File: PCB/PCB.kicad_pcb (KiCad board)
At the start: 4 copper layers, 104.1 x 104.1 mm, 113 parts, among them J1 Conn_01x06_Female, J2 09252306841, U1 Hx711, U10 Hx711, U11 Hx711, U12 Hx711, U13 74HC165, U15 LT3042xMSE, U16 74HC165, U2 Hx711, U3 Hx711, U4 Hx711, U5 Hx711, U6 Hx711, U7 Hx711, U8 Hx711, U9 Hx711

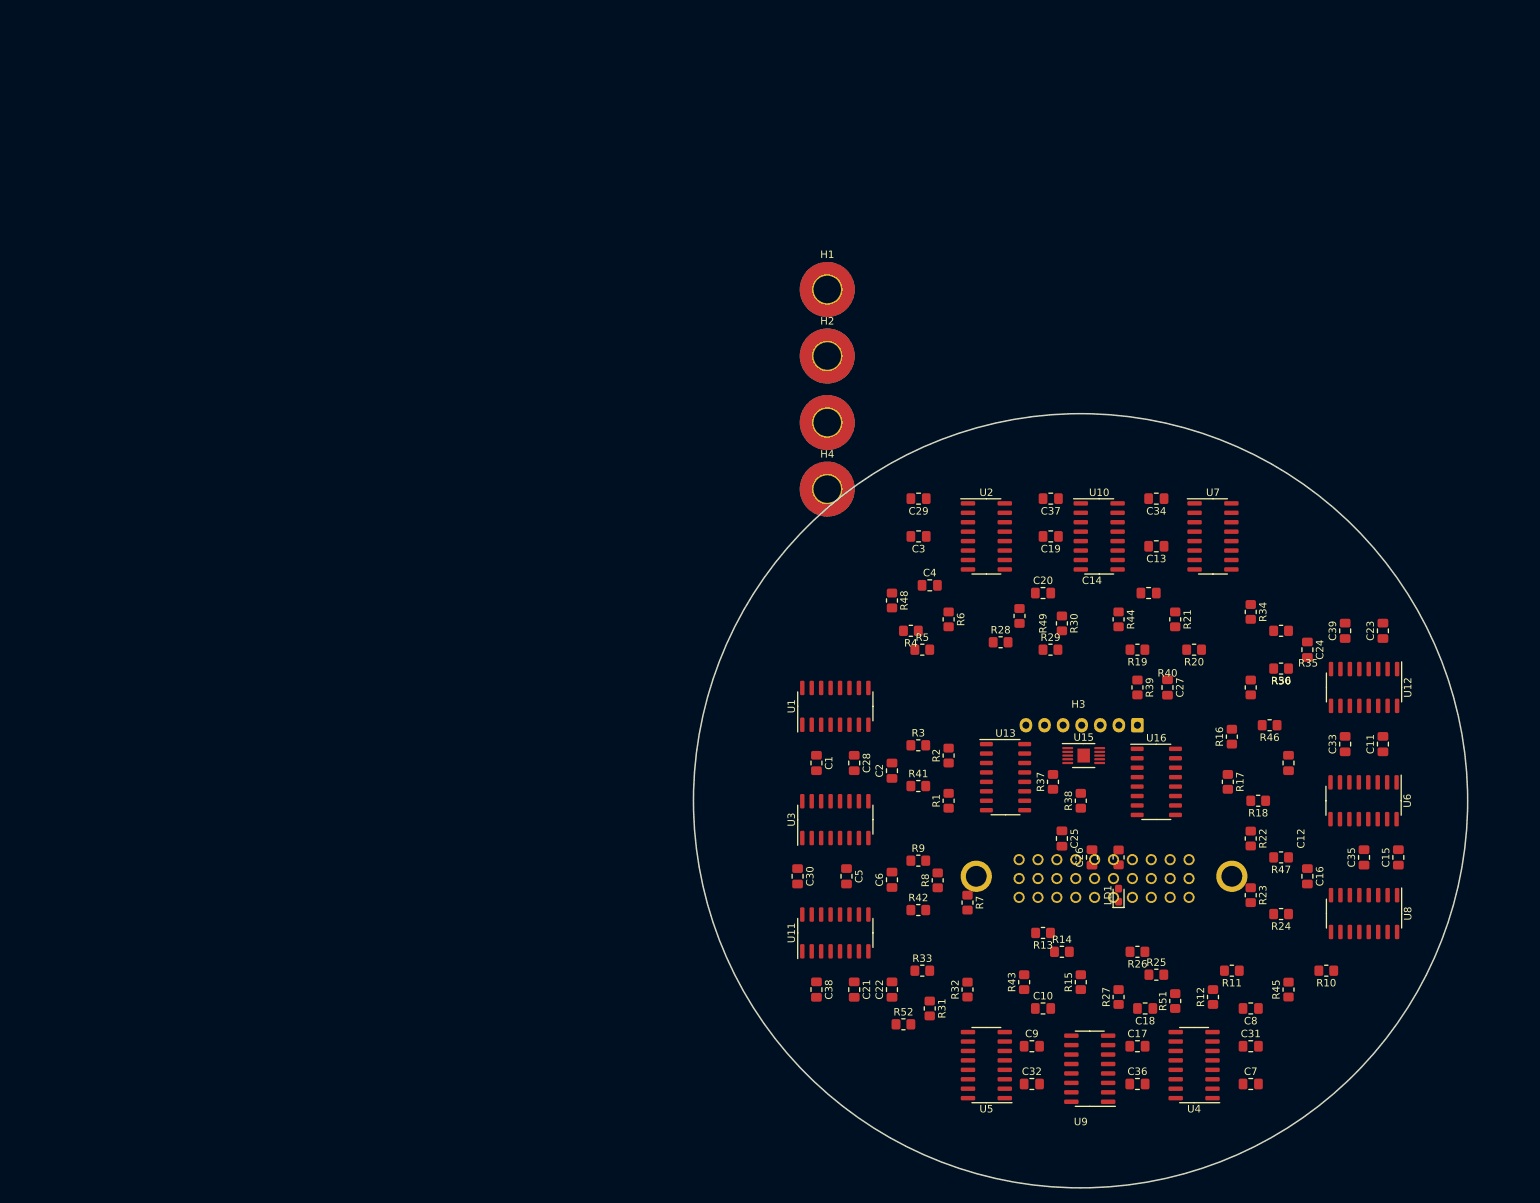
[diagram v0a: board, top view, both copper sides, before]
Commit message: Updates to layout
Started using radial, sides are going everywhere.
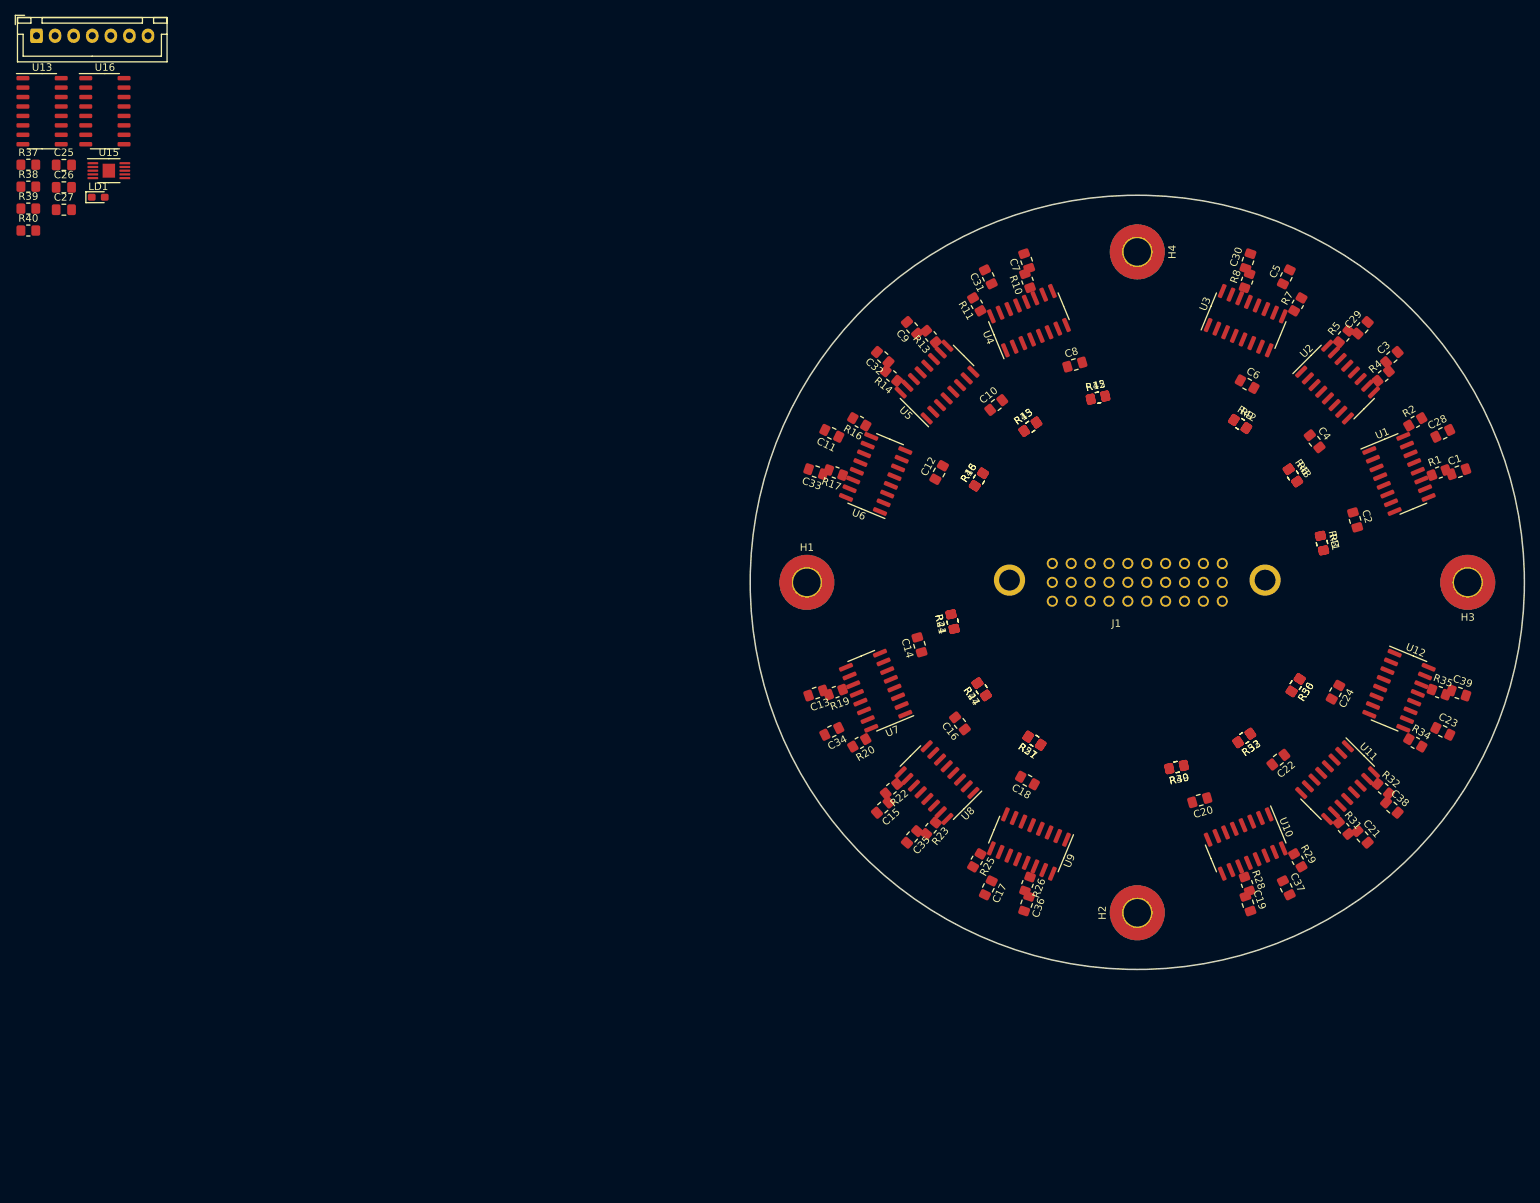
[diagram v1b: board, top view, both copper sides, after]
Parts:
- J1: moved to F.Cu
- moved J1 174.7 mm to (11.9, 16.5), turned to 0 degrees
- moved R40 169.2 mm to (10.8, 42.7), turned to 0 degrees
- moved U16 167.8 mm to (21.1, 26.6)
- moved LD1 166.3 mm to (20.2, 38.2), turned to 0 degrees
- moved C26 165.1 mm to (15.6, 36.9), turned to 0 degrees
- moved R38 163.9 mm to (10.8, 36.8), turned to 0 degrees
- moved R39 162.5 mm to (10.8, 39.7), turned to 0 degrees
- moved C25 162.0 mm to (15.6, 33.9), turned to 0 degrees
- moved C27 161.8 mm to (15.6, 39.9), turned to 0 degrees
- moved R37 160.9 mm to (10.8, 33.8), turned to 0 degrees
- moved U13 157.5 mm to (12.7, 26.6)
- moved U15 152.9 mm to (21.7, 34.6)
- moved C7 114.7 mm to (145.1, 46.8), turned to 109 degrees
- moved C31 109.3 mm to (140.0, 48.9), turned to 116 degrees
- moved U4 102.6 mm to (145.4, 54.8), turned to 112.5 degrees
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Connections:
- J2 pad MH1: unconnected-(J2-PadMH1) -> GND
- J2 pad MH2: unconnected-(J2-PadMH2) -> GND

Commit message: Updated pcb
Working on setting the positions to be adequate before tracing
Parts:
- moved U13 168.4 mm to (158.1, 111.5), turned to 175 degrees
- moved J1 165.3 mm to (155.1, 99.1)
- moved R40 150.7 mm to (156.5, 81.3)
- moved U16 146.9 mm to (161.9, 68.5), turned to -5 degrees
- moved LD1 146.5 mm to (160.9, 79.3), turned to 90 degrees
- moved C25 139.1 mm to (148.5, 75.0)
- moved C26 139.1 mm to (148.5, 78.0)
- moved C27 139.1 mm to (148.5, 81.0)
- moved R37 139.1 mm to (143.7, 74.9)
- moved R38 139.1 mm to (143.7, 77.9)
- moved R39 139.1 mm to (143.7, 80.8)
- moved U15 139.1 mm to (154.5, 75.7)
- moved R20 20.3 mm to (133.7, 94.6), turned to 100 degrees
- moved R29 20.3 mm to (164.6, 116.3), turned to -170 degrees
- moved R11 20.3 mm to (155.4, 63.7), turned to 10 degrees
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
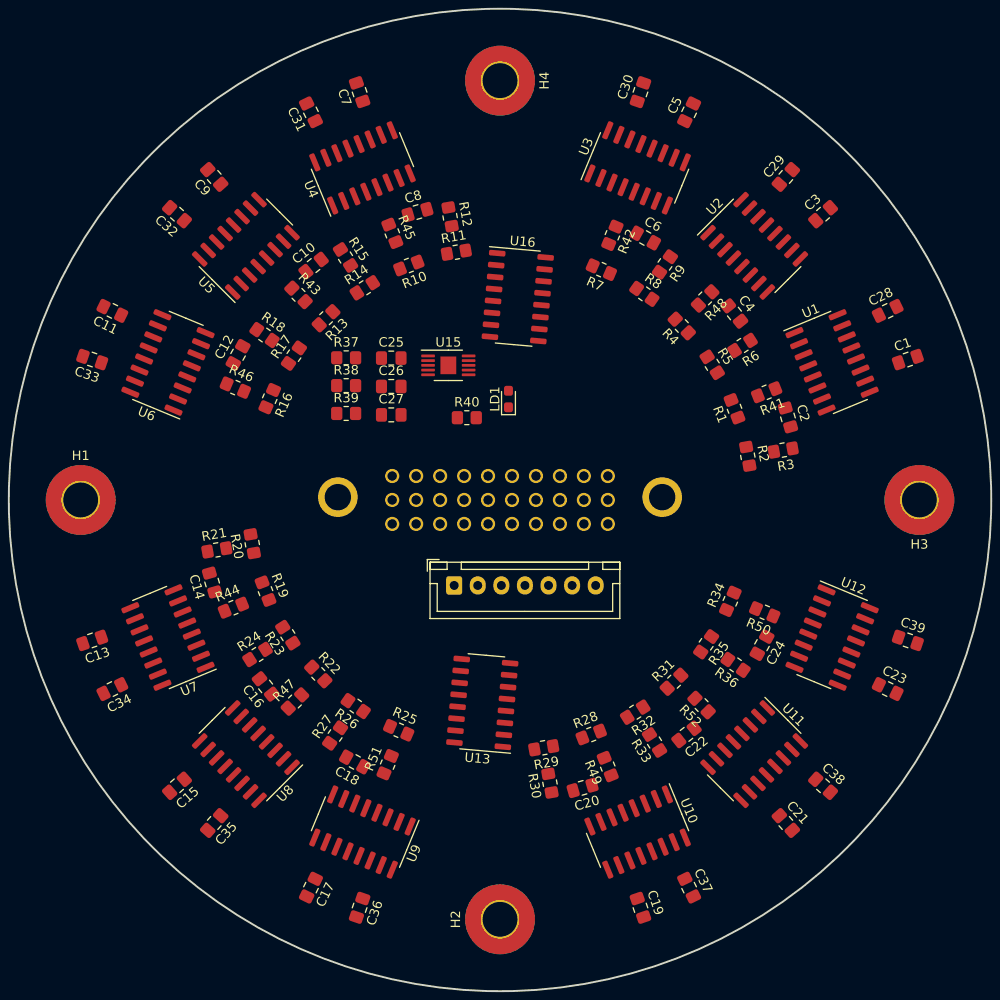
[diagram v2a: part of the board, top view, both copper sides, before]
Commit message: Connector update
Changed the connector I found to a db25 and adjusted the radius of components to compensate
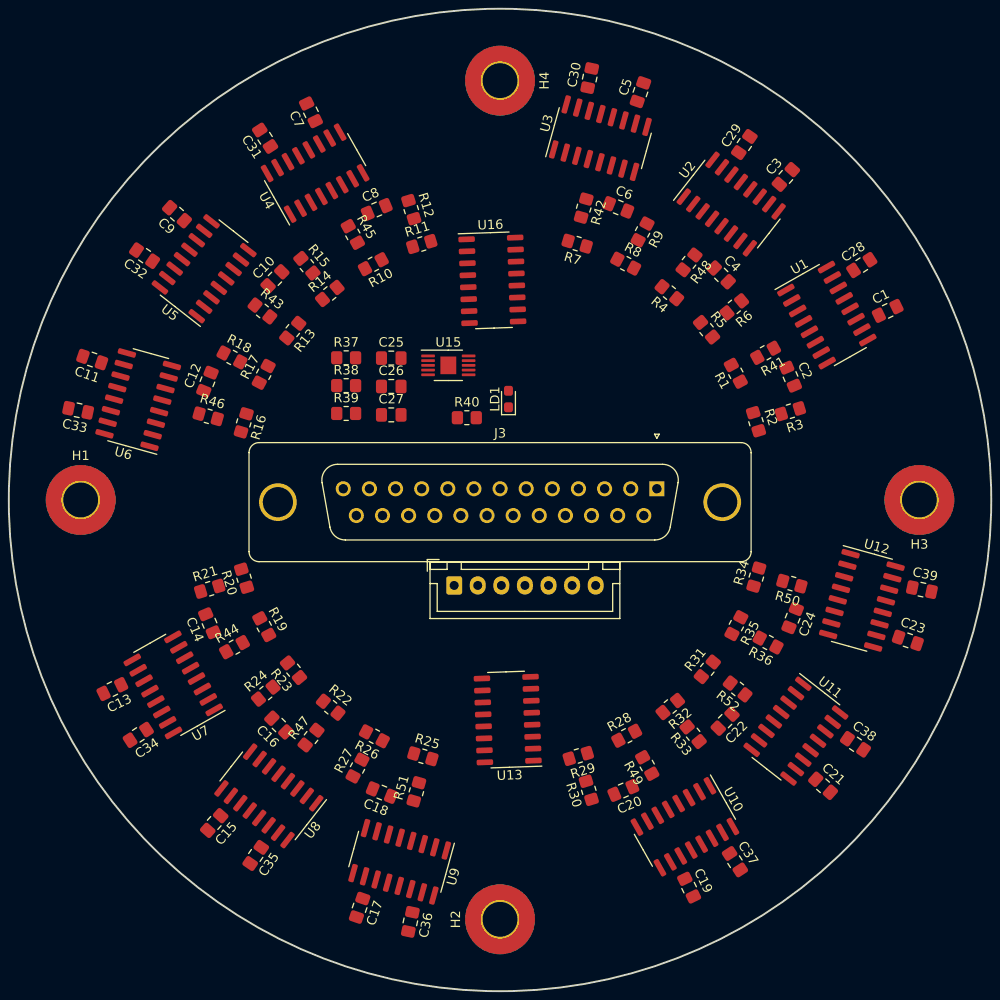
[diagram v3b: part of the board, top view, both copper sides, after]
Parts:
- removed J2: 09252306841, 09252306841:09252306841
- added J3: DB25_Receptacle_MountingHoles, Connector_Dsub:DSUB-25_Female_Vertical_P2.77x2.84mm_MountingHoles, F.Cu at (176.6, 88.8)
- moved C36 5.58 mm to (150.5, 134.7), turned to -102 degrees
- moved C30 5.58 mm to (169.5, 45.3), turned to 78 degrees
- moved C33 5.58 mm to (115.3, 80.5), turned to 168 degrees
- moved C39 5.58 mm to (204.7, 99.5), turned to -12 degrees
- moved C15 5.58 mm to (129.7, 124.2), turned to -131.5 degrees
- moved C21 5.58 mm to (194.2, 120.3), turned to -41.5 degrees
- moved C3 5.58 mm to (190.3, 55.8), turned to 48.5 degrees
- moved C9 5.58 mm to (125.8, 59.7), turned to 138.5 degrees
- moved C34 5.58 mm to (121.7, 114.9), turned to -147 degrees
- moved C28 5.58 mm to (198.3, 65.1), turned to 33 degrees
- moved C31 5.58 mm to (135.1, 51.7), turned to 123 degrees
- moved C37 5.58 mm to (184.9, 128.3), turned to -57 degrees
- moved C38 5.58 mm to (197.7, 115.9), turned to -34.5 degrees
- moved C32 5.58 mm to (122.3, 64.1), turned to 145.5 degrees
- moved C35 5.58 mm to (134.1, 127.7), turned to -124.5 degrees
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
